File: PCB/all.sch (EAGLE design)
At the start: 116 parts, among them J1 ISP Programmer, J8 BL-HP20AUW2C, U1 ATTINY1634MLF20, U2 3.3V_REG, U3 MPU-6050-1, U4 BQ51013B_RHL_20, U5 MCP73831, U6 AL8805, U7 BQ51013B_RHL_20, U8 BQ51013B_RHL_20, U9 BQ51013B_RHL_20

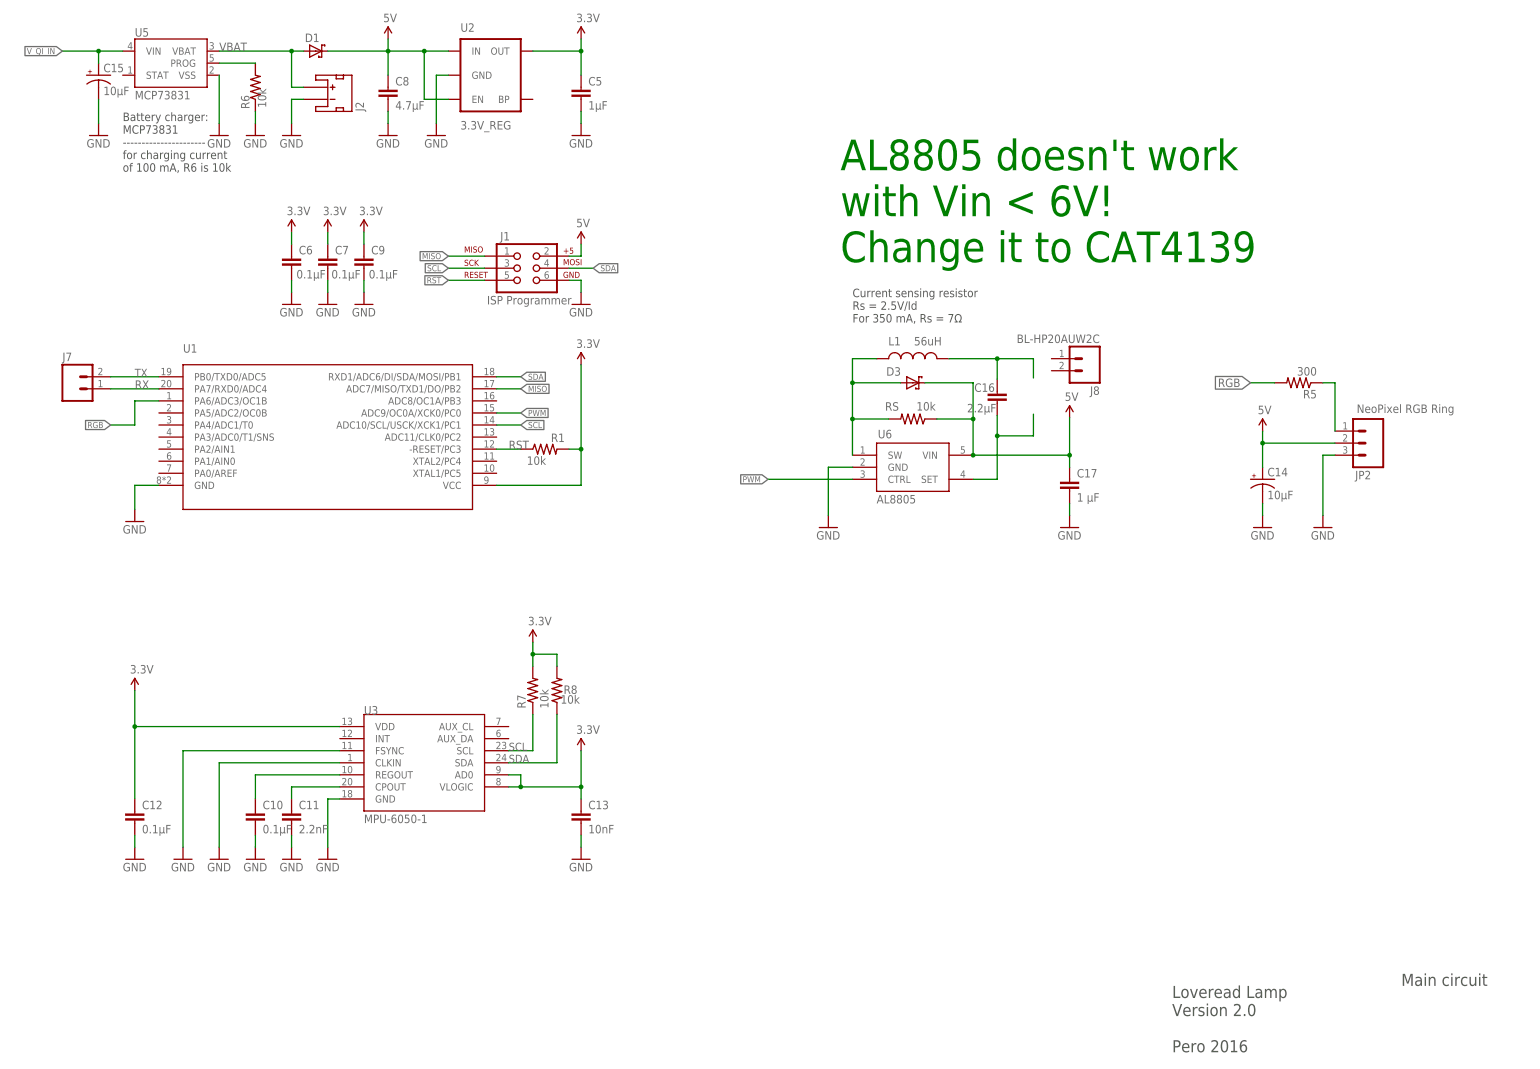
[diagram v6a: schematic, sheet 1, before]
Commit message: LED driver changed
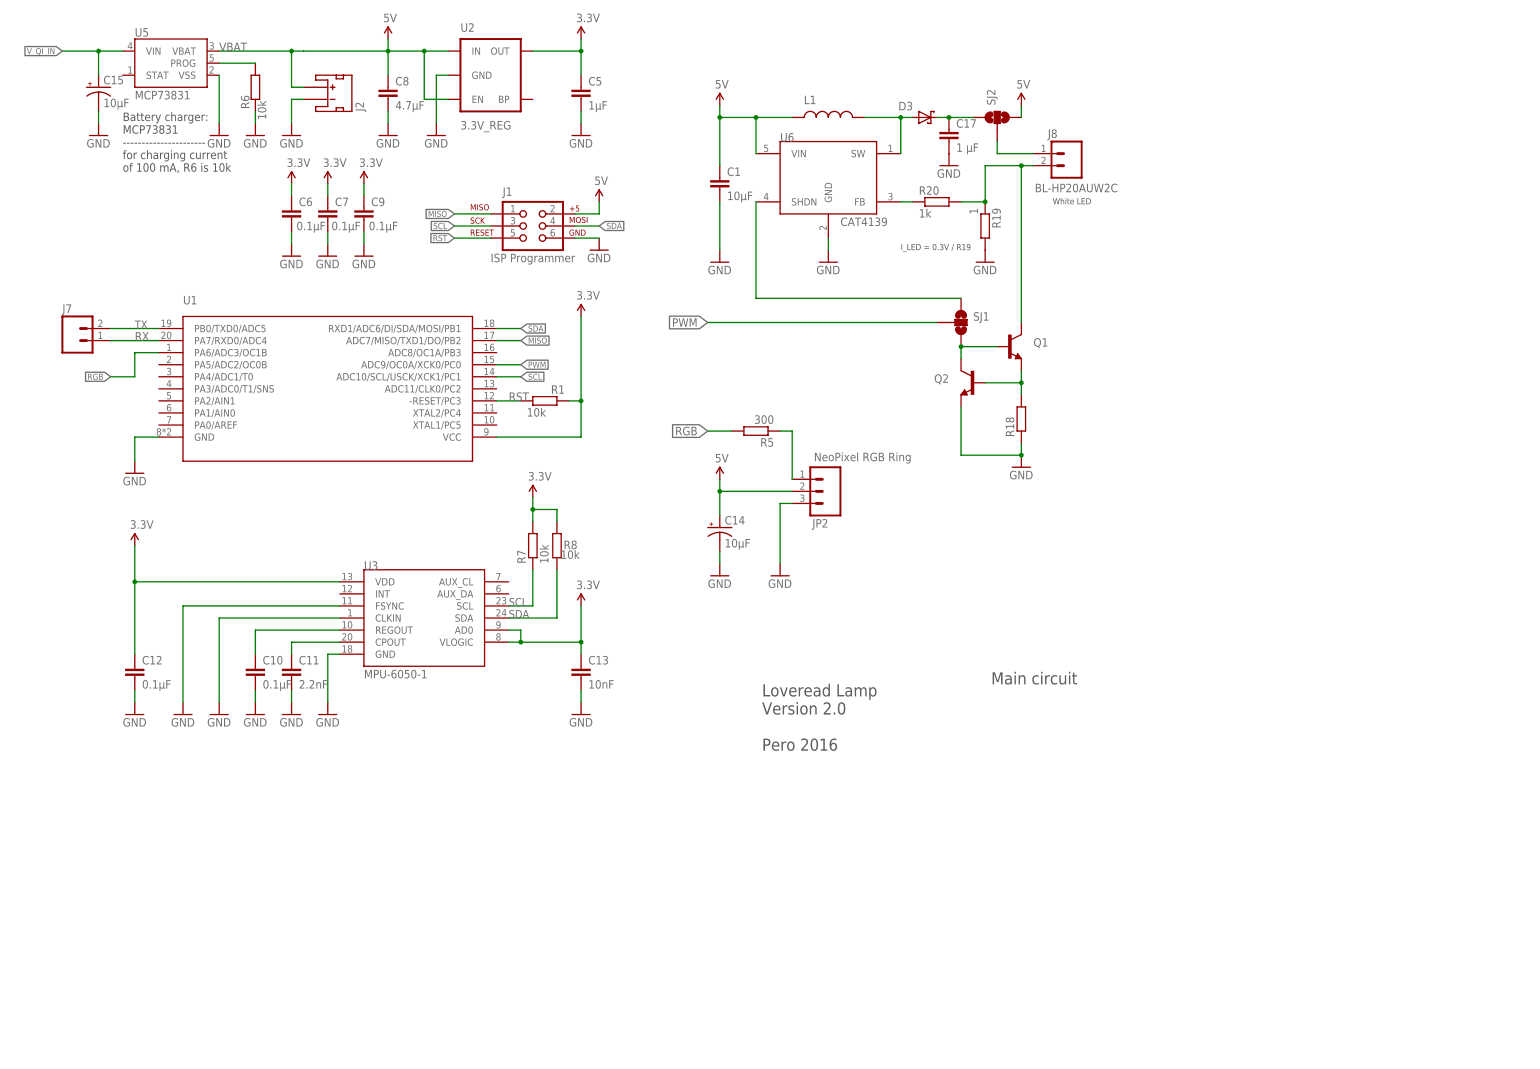
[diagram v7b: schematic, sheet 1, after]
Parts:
- removed C16: 2.2μF, SparkFun:CAP0603-CAP
- removed D1: SMF5.0AT1, diode:SMF5.0AT1
- removed RS: 10k, rcl:R-US_R0603
- added C1: 10μF, rcl:C-EUC0603
- added Q1, Q2: (no value), SparkFun-DiscreteSemi:TRANSISTOR_NPNSOT23-3
- added R18: (no value), rcl:R-EU_R0603
- added R19: 1, resistor:R-EU_R0603
- added R20: 1k, resistor:R-EU_R0603
- added SJ1, SJ2: (no value), SparkFun-Retired:SOLDERJUMPER_2WAYPASTE2&3
- L1: value 56uH -> 22uH
- R1, R5, R6, R7, R8: device rcl:R-US_R0603 -> rcl:R-EU_R0603
- U6: value AL8805 -> CAT4139; device pero_library2:AL8805 -> pero_library:CAT4139
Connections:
- removed net ANODE: C16.2, U6.SET
- removed net CATHODE: C16.1, L1.2
- new net N$2: Q1.E, Q2.B, R18.2
- new net N$3: Q1.B, Q2.C, SJ1.3
- new net N$4: SJ1.1, U6.SHDN
- new net N$62: J8.1, SJ2.2
- new net N$63: D3.A, L1.2, U6.SW
- new net N$64: C17.1, D3.C, SJ2.1
- new net N$65: R20.1, U6.FB
- net 5V: now also C1.1, L1.1, SJ2.3; no longer C17.1, D1.C, D3.C, RS.1
- net GND: now also C1.2, Q2.E, R18.1, R19.2
- net N$18: now also J8.2, Q1.C, R19.1, R20.2; no longer D3.A, L1.1, RS.2, U6.SW
- net PWM: now also SJ1.2; no longer U6.CTRL
- net VBAT: no longer D1.A
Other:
- note added: "I_LED = 0.3V / R19"
- note added: "White LED"
- note removed: "AL8805 doesn't work with Vin < 6V! Change it to CAT4139"
- note removed: "Current sensing resistor Rs = 2.5V/Id For 350 mA, Rs = 7Ω"
- moved on the sheet: C10, C11, C12, C13, C14, C15, C17, C6, C7, C9, D3, J1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

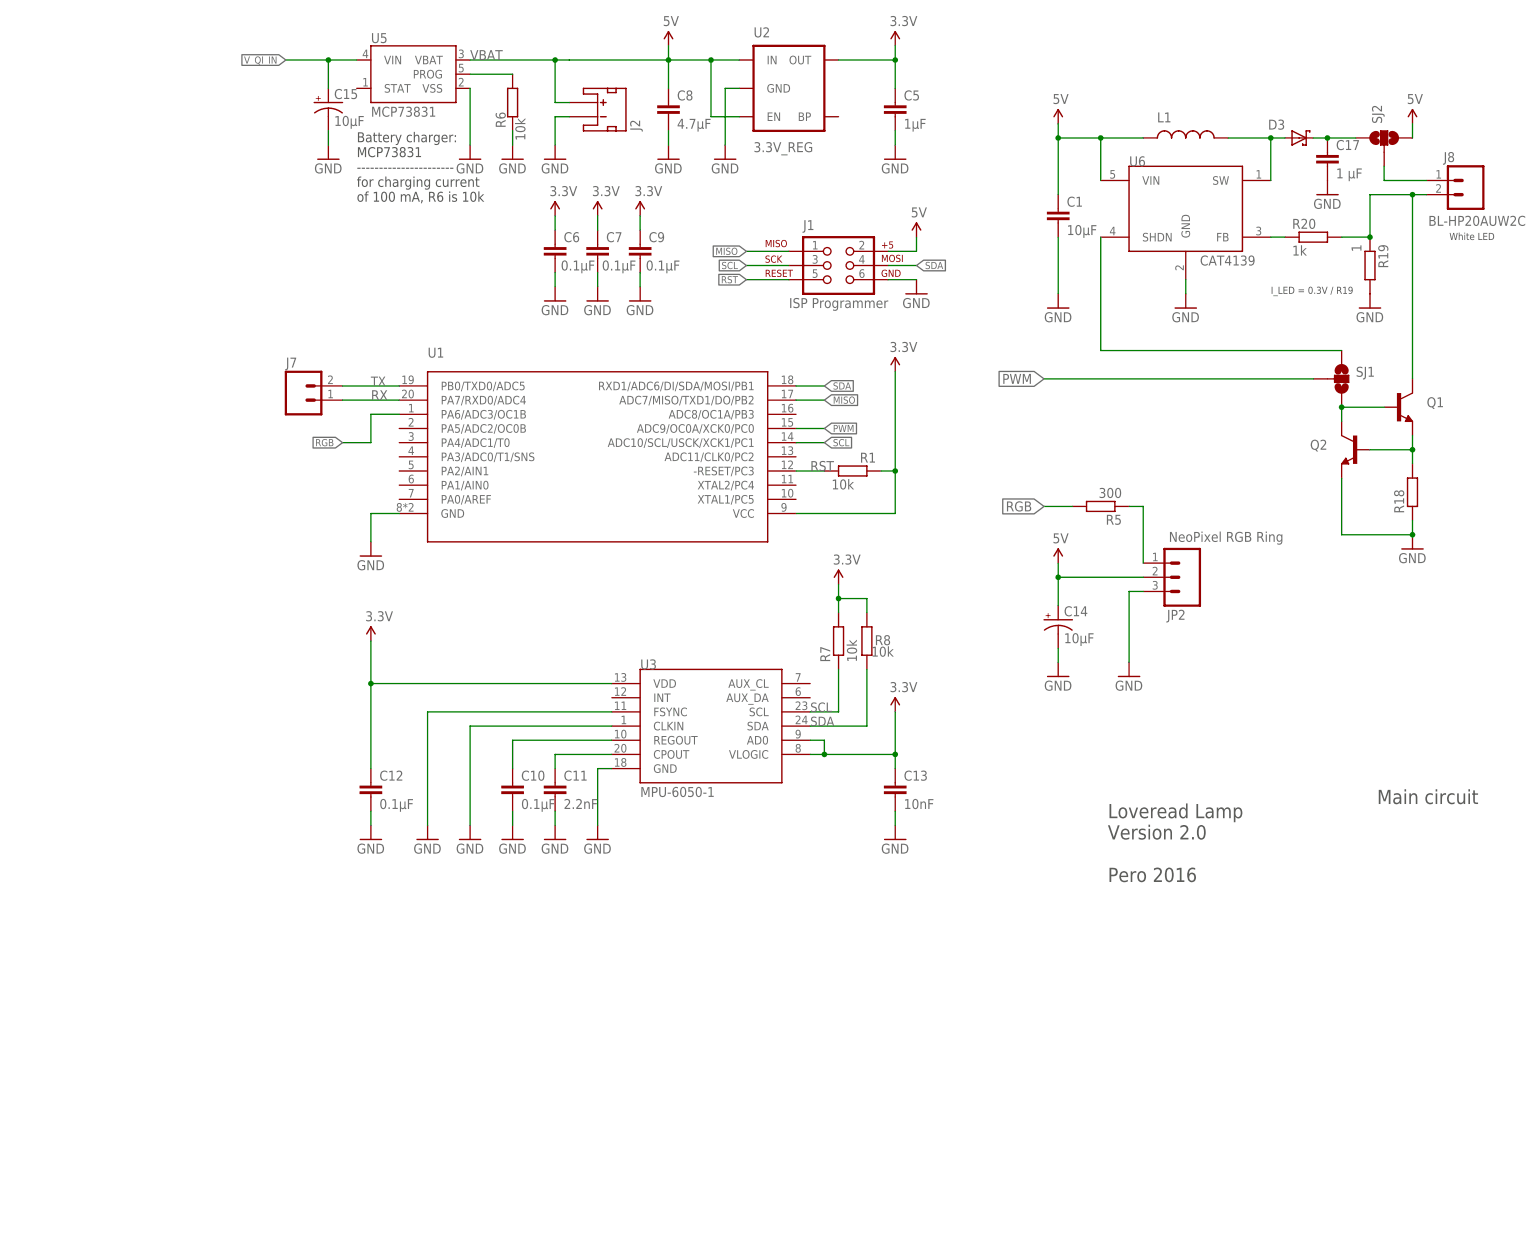
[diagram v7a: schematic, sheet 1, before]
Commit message: Adds buck converter
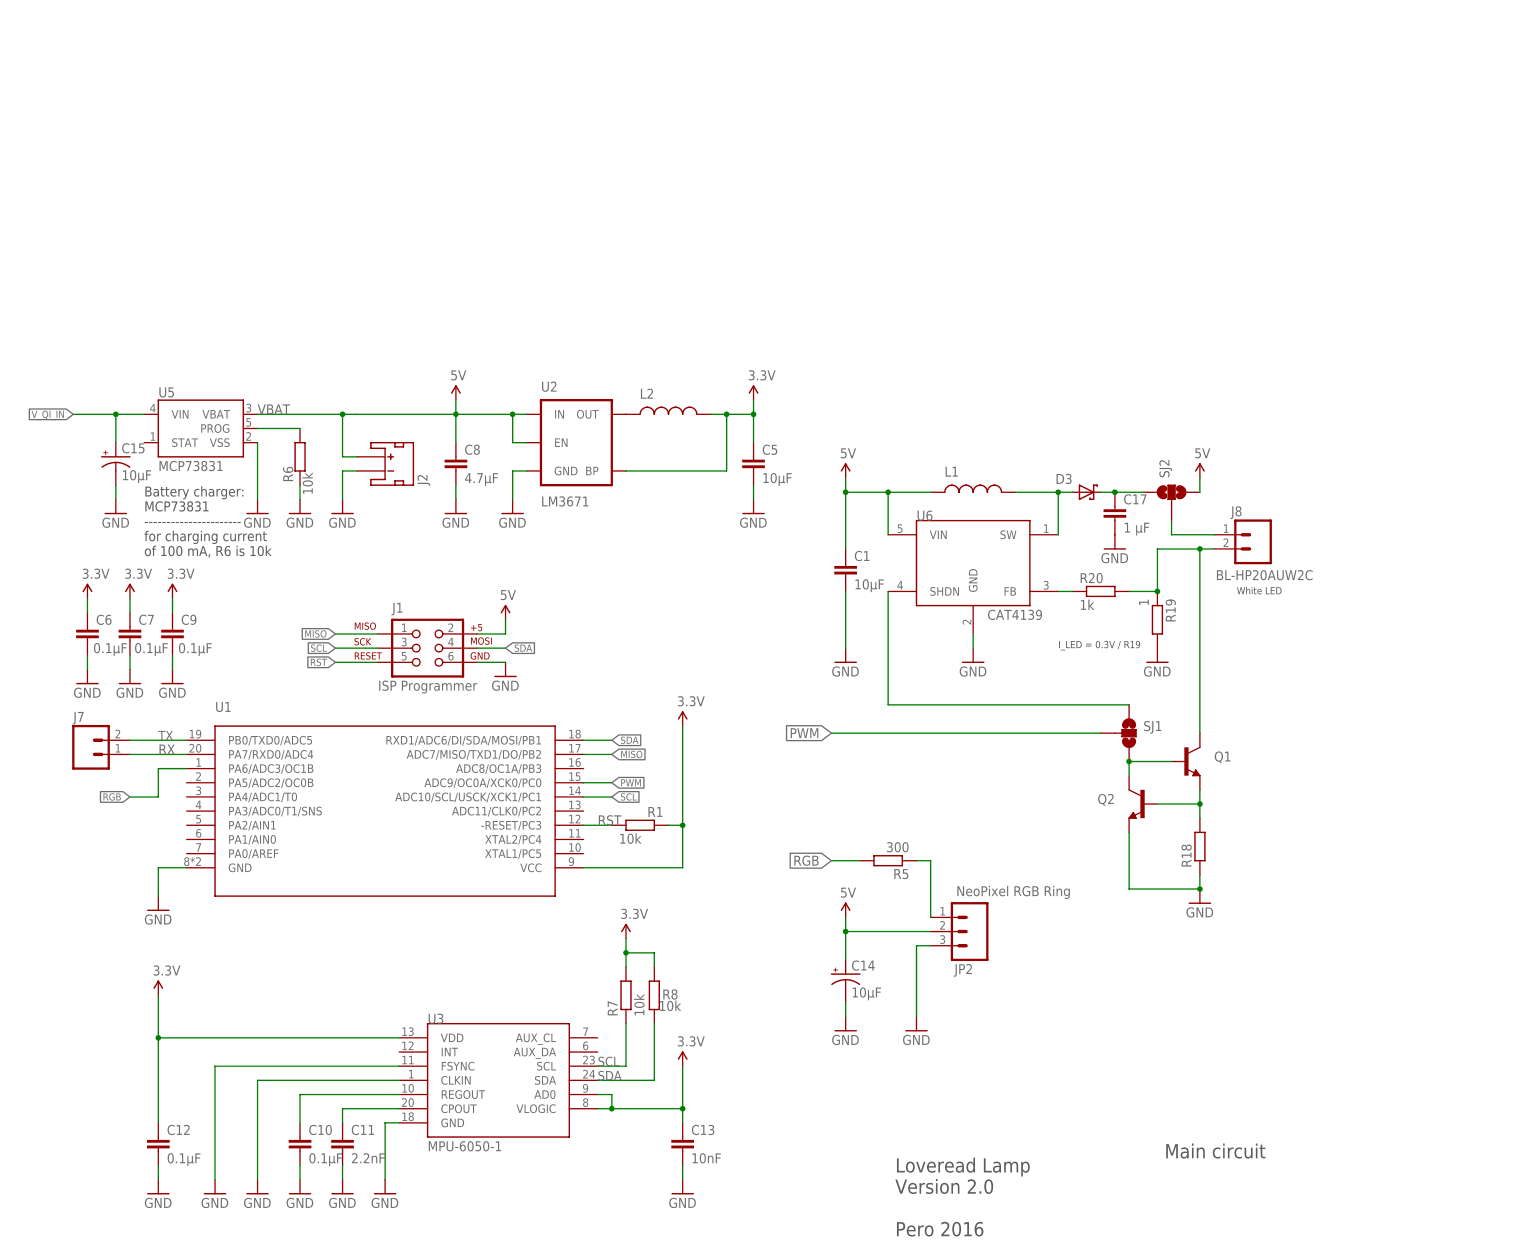
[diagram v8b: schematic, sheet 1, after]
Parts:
- added L2: 22uH, SparkFun-Passives:INDUCTORSDR0403-560KL
- C5: value 1μF -> 10μF
- J2: value (none) -> LIPO-BATTERY-CONNECTOR; device SparkFun-Connectors:JST_2MM_MALE -> pero_library:LIPO-BATTERY-CONNECTOR
- U2: value 3.3V_REG -> LM3671; device SparkFun:V_REG_LDOSMD -> pero_library:LM36713.3V
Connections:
- new net N$66: L2.1, U2.OUT
- net 3.3V: now also L2.2, U2.BP; no longer U2.OUT
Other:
- moved on the sheet: C1, C10, C11, C12, C13, C14, C15, C17, C5, C6, C7, C8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
